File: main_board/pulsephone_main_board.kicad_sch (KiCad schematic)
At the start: 88 parts, among them J1 USB_C_Receptacle_USB2.0_14P, J2 Conn_01x05, J3 Conn_2Rows-35Pins_MountingPin, J4 Conn_2Rows-35Pins_MountingPin, J5 Conn_2Rows-35Pins_MountingPin, J7 Micro_SD_Card_Det1, SW1 SW_Push, SW2 SW_Push, U1 XL1509-3.3, U2 PCM5102APWR, U4 TPS63020DSJR/3.7V Reg, U5 TP4056-42-ESOP8

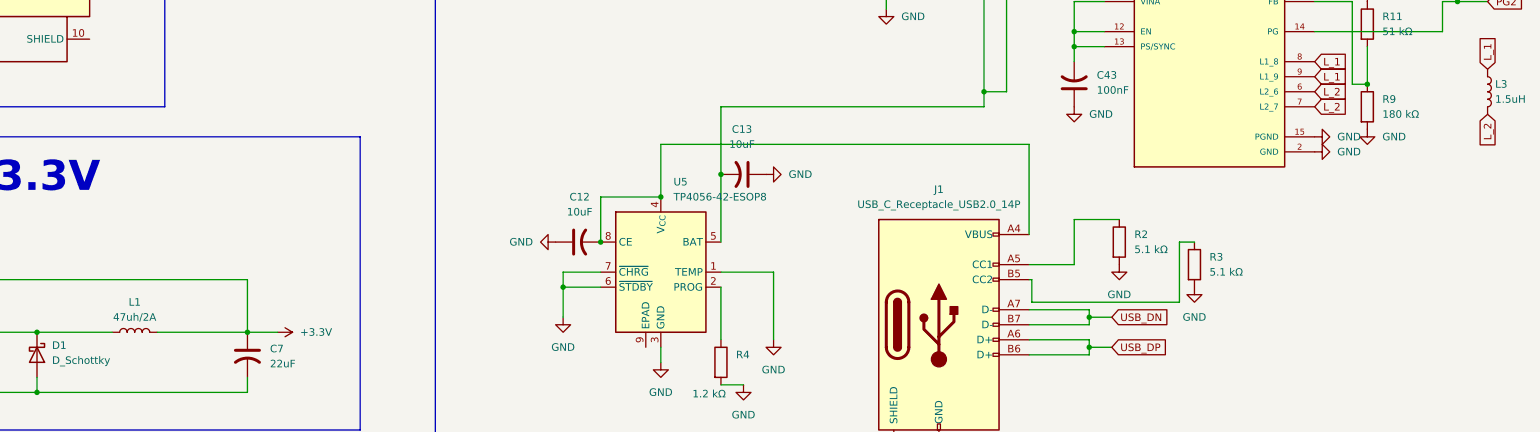
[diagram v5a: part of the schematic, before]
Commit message: footprint size adjustments for better part compatibility when ordering
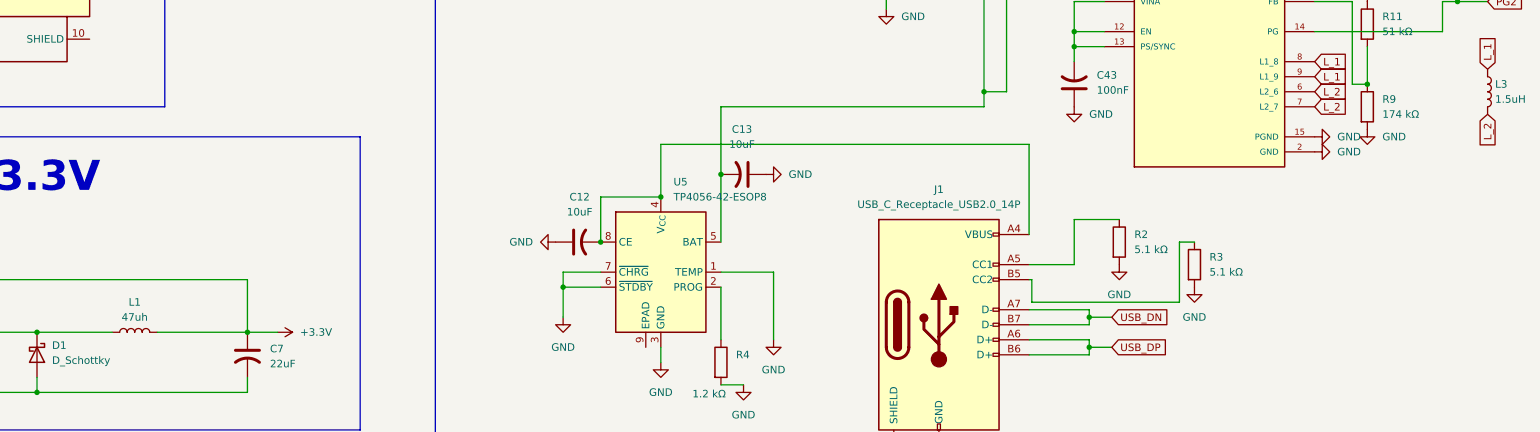
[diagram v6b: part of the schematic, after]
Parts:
- BT1: footprint Connector_PinHeader_1.00mm:PinHeader_1x02_P1.00mm_Horizontal -> Connector_PinHeader_2.54mm:PinHeader_1x02_P2.54mm_Horizontal
- C1, C10, C11, C14, C15, C16, C17, C18, C19, C20, C21, C22, C23, C24, C25, C26, C27, C28, C29, C30, C31, C32, C35, C36, C37, C7, C8, C9: footprint Capacitor_SMD:C_0603_1608Metric -> Capacitor_SMD:C_0805_2012Metric
- J2: footprint Connector_PinHeader_1.00mm:PinHeader_1x05_P1.00mm_Horizontal -> Connector_PinHeader_2.54mm:PinHeader_1x05_P2.54mm_Horizontal
- L1: value 47uh/2A -> 47uh; footprint Inductor_SMD:L_APV_APH0630 -> Inductor_SMD:L_KOHERelec_MDA7030
- R9: value 180 kΩ -> 174 kΩ
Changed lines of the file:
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@@
 			)
 		)
-		(property "Footprint" "Capacitor_SMD:C_0603_1608Metric"
+		(property "Footprint" "Capacitor_SMD:C_0805_2012Metric"
 			(at 458.47 128.27 0)
 			(effects
@@
 			)
 		)
-		(property "Footprint" "Capacitor_SMD:C_0603_1608Metric"
+		(property "Footprint" "Capacitor_SMD:C_0805_2012Metric"
 			(at 505.46 128.27 0)
 			(effects
@@
 			)
 		)
-		(property "Footprint" "Capacitor_SMD:C_0603_1608Metric"
+		(property "Footprint" "Capacitor_SMD:C_0805_2012Metric"
 			(at 792.48 363.22 0)
 			(effects
@@
 			)
 		)
-		(property "Footprint" "Capacitor_SMD:C_0603_1608Metric"
+		(property "Footprint" "Capacitor_SMD:C_0805_2012Metric"
 			(at 600.71 441.96 0)
 			(effects
@@
 			)
 		)
-		(property "Footprint" "Capacitor_SMD:C_0603_1608Metric"
+		(property "Footprint" "Capacitor_SMD:C_0805_2012Metric"
 			(at 712.47 100.33 0)
 			(effects
@@
 			)
 		)
-		(property "Footprint" "Capacitor_SMD:C_0603_1608Metric"
+		(property "Footprint" "Capacitor_SMD:C_0805_2012Metric"
 			(at 792.48 355.6 0)
 			(effects
@@
 			)
 		)
-		(property "Footprint" "Capacitor_SMD:C_0603_1608Metric"
+		(property "Footprint" "Capacitor_SMD:C_0805_2012Metric"
 			(at 429.26 128.27 0)
 			(effects
@@
 			)
 		)
-		(property "Footprint" "Capacitor_SMD:C_0603_1608Metric"
+		(property "Footprint" "Capacitor_SMD:C_0805_2012Metric"
 			(at 533.4 495.3 0)
 			(effects
@@
 			)
 		)
-		(property "Footprint" "Capacitor_SMD:C_0603_1608Metric"
+		(property "Footprint" "Capacitor_SMD:C_0805_2012Metric"
 			(at 534.67 128.27 0)
 			(effects
@@
 			)
 		)
-		(property "Footprint" "Capacitor_SMD:C_0603_1608Metric"
+		(property "Footprint" "Capacitor_SMD:C_0805_2012Metric"
 			(at 726.44 100.33 0)
 			(effects
@@
 			)
 		)
-		(property "Footprint" "Capacitor_SMD:C_0603_1608Metric"
+		(property "Footprint" "Capacitor_SMD:C_0805_2012Metric"
 			(at 741.68 100.33 0)
 			(effects
@@
 			)
 		)
-		(property "Footprint" "Capacitor_SMD:C_0603_1608Metric"
+		(property "Footprint" "Capacitor_SMD:C_0805_2012Metric"
 			(at 792.48 370.84 0)
 			(effects
@@
 			)
 		)
-		(property "Footprint" "Capacitor_SMD:C_0603_1608Metric"
+		(property "Footprint" "Capacitor_SMD:C_0805_2012Metric"
 			(at 473.71 128.27 0)
 			(effects
@@
 			)
 		)
-		(property "Footprint" "Capacitor_SMD:C_0603_1608Metric"
+		(property "Footprint" "Capacitor_SMD:C_0805_2012Metric"
 			(at 590.55 518.16 0)
 			(effects
@@
 			)
 		)
-		(property "Footprint" "Capacitor_SMD:C_0603_1608Metric"
+		(property "Footprint" "Capacitor_SMD:C_0805_2012Metric"
 			(at 651.51 100.33 0)
 			(effects
@@
 			)
 		)
-		(property "Footprint" "Capacitor_SMD:C_0603_1608Metric"
+		(property "Footprint" "Capacitor_SMD:C_0805_2012Metric"
 			(at 665.48 100.33 0)
 			(effects
@@
 			)
 		)
-		(property "Footprint" "Capacitor_SMD:C_0603_1608Metric"
+		(property "Footprint" "Capacitor_SMD:C_0805_2012Metric"
 			(at 636.27 100.33 0)
 			(effects
@@
 			)
 		)
-		(property "Footprint" "Connector_PinHeader_1.00mm:PinHeader_1x02_P1.00mm_Horizontal"
+		(property "Footprint" "Connector_PinHeader_2.54mm:PinHeader_1x02_P2.54mm_Horizontal"
 			(at 708.66 374.396 90)
 			(effects
@@
 			)
 		)
-		(property "Datasheet" "~"
+		(property "Datasheet" ""
 			(at 708.66 374.396 90)
 			(effects
@@
 			)
 		)
-		(property "Description" "Multiple-cell battery"
+		(property "Description" ""
 			(at 708.66 375.92 0)
 			(effects
@@
 			)
 		)
-		(property "Footprint" "Capacitor_SMD:C_0603_1608Metric"
+		(property "Footprint" "Capacitor_SMD:C_0805_2012Metric"
 			(at 444.5 128.27 0)
 			(effects
@@
 			)
 		)
-		(property "Value" "180 kΩ"
+		(property "Value" "174 kΩ"
 			(at 792.48 401.3199 0)
 			(effects
@@
 			)
 		)
-		(property "Footprint" "Capacitor_SMD:C_0603_1608Metric"
+		(property "Footprint" "Capacitor_SMD:C_0805_2012Metric"
 			(at 590.55 502.92 0)
 			(effects
@@
 			)
 		)
-		(property "Footprint" "Capacitor_SMD:C_0603_1608Metric"
+		(property "Footprint" "Capacitor_SMD:C_0805_2012Metric"
 			(at 383.54 128.27 0)
 			(effects
@@
 			)
 		)
-		(property "Footprint" "Capacitor_SMD:C_0603_1608Metric"
+		(property "Footprint" "Capacitor_SMD:C_0805_2012Metric"
 			(at 490.22 128.27 0)
 			(effects
@@
 			)
 		)
-		(property "Footprint" "Capacitor_SMD:C_0603_1608Metric"
+		(property "Footprint" "Capacitor_SMD:C_0805_2012Metric"
 			(at 590.55 510.54 0)
 			(effects
@@
 			)
 		)
-		(property "Footprint" "Capacitor_SMD:C_0603_1608Metric"
+		(property "Footprint" "Capacitor_SMD:C_0805_2012Metric"
 			(at 397.51 128.27 0)
 			(effects
@@
 			)
 		)
-		(property "Footprint" "Connector_PinHeader_1.00mm:PinHeader_1x05_P1.00mm_Horizontal"
+		(property "Footprint" "Connector_PinHeader_2.54mm:PinHeader_1x05_P2.54mm_Horizontal"
 			(at 289.56 359.41 0)
 			(effects
@@
 			)
 		)
-		(property "Datasheet" "~"
+		(property "Datasheet" ""
 			(at 289.56 359.41 0)
 			(effects
@@
 			)
 		)
-		(property "Description" "Generic connector, single row, 01x05, script generated (kicad-library-utils/schlib/autogen/connector/)"
+		(property "Description" ""
 			(at 289.56 359.41 0)
 			(effects
@@
 			)
 		)
-		(property "Footprint" "Capacitor_SMD:C_0603_1608Metric"
+		(property "Footprint" "Capacitor_SMD:C_0805_2012Metric"
 			(at 521.97 441.96 0)
 			(effects
@@
 			)
 		)
-		(property "Footprint" "Capacitor_SMD:C_0603_1608Metric"
+		(property "Footprint" "Capacitor_SMD:C_0805_2012Metric"
 			(at 519.43 128.27 0)
 			(effects
@@
 			)
 		)
-		(property "Footprint" "Capacitor_SMD:C_0603_1608Metric"
+		(property "Footprint" "Capacitor_SMD:C_0805_2012Metric"
 			(at 412.75 128.27 0)
 			(effects
@@
 			)
 		)
-		(property "Footprint" "Capacitor_SMD:C_0603_1608Metric"
+		(property "Footprint" "Capacitor_SMD:C_0805_2012Metric"
 			(at 680.72 100.33 0)
 			(effects
@@
 			)
 		)
-		(property "Value" "47uh/2A"
+		(property "Value" "47uh"
 			(at 581.66 435.61 90)
 			(effects
@@
 			)
 		)
-		(property "Footprint" "Inductor_SMD:L_APV_APH0630"
+		(property "Footprint" "Inductor_SMD:L_KOHERelec_MDA7030"
 			(at 581.66 438.15 0)
 			(effects
@@
 			)
 		)
-		(property "Datasheet" "~"
+		(property "Datasheet" ""
 			(at 581.66 438.15 0)
 			(effects
@@
 			)
 		)
-		(property "Description" "Inductor"
+		(property "Description" ""
 			(at 581.66 438.15 0)
 			(effects
@@
 			)
 		)
-		(property "Footprint" "Capacitor_SMD:C_0603_1608Metric"
+		(property "Footprint" "Capacitor_SMD:C_0805_2012Metric"
 			(at 697.23 100.33 0)
 			(effects

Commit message: final review change (board was ordered, prod ready verSion)
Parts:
- added AUD-L1, AUD-R1: TestPoint, TestPoint:TestPoint_Pad_1.0x1.0mm, symbol Connector:TestPoint
- added I2C3-SCL1, I2C3-SDA1: TestPoint, TestPoint:TestPoint_Pad_D1.0mm, symbol Connector:TestPoint
- 3.3V1, 5V1, CLK-N1, CLK-P1, D0-N1, D0-P1, D1-N1, D1-P1, D2-N1, D2-P1, D3-N1, D3-P1, GND1, VBAT1: footprint TestPoint:TestPoint_Pad_1.0x1.0mm -> TestPoint:TestPoint_Pad_D1.0mm
- J1: footprint Connector_USB:USB_C_Receptacle_Amphenol_12401548E4-2A -> Connector_USB:USB_C_Receptacle_HRO_TYPE-C-31-M-12
- ON/OFF1: renamed from SW2; footprint Button_Switch_SMD:SW_Tactile_SPST_NO_Straight_CK_PTS636Sx25SMTRLFS -> SSSS810701:SSSS810701; symbol Switch:SW_Push -> SSSS810701:SSSS810701; Availability (none) -> In Stock; Check_prices (none) -> https://www.snapeda.com/parts/SSSS810701/ALPS/view-part/?re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; Description_1 (none) -> Slide Switch • Rating (max.): 0.3 A 5 VDC • Poles: 1 • Posi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; MF (none) -> ALPS; MP (none) -> SSSS810701; Package (none) -> None; Price (none) -> None; SnapEDA_Link (none) -> https://www.snapeda.com/parts/SSSS810701/ALPS/view-part/?re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
- RESET1: renamed from SW1; footprint Button_Switch_SMD:SW_Tactile_SPST_NO_Straight_CK_PTS636Sx25SMTRLFS -> Button_Switch_SMD:SW_Push_1P1T-SH_NO_CK_KMR2xxG
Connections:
- net GND: now also J1.S1 (SHIELD), J7.10 (SHIELD), U5.9 (EPAD)
- net GNDCHASSIS: no longer J1.S1 (SHIELD)
- net I2C3_SCL: now also I2C3-SCL1.1
- net I2C3_SDA: now also I2C3-SDA1.1
- net ONOFF: now also ON/OFF1.3; no longer ON/OFF1.2
- net at J5.8 (Pin_8), U2.6 (OUTL): now also AUD-L1.1
- net at J5.9 (Pin_9), U2.7 (OUTR): now also AUD-R1.1
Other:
- moved on the sheet: ON/OFF1

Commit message: restart project for summer, misc changes
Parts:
- removed D1: D_Schottky, Diode_SMD:D_SMA, symbol Device:D_Schottky
- removed L1: 47uh, Inductor_SMD:L_KOHERelec_MDA7030, symbol Device:L
- removed U1: XL1509-3.3, Package_SO:SOIC-8_3.9x4.9mm_P1.27mm, symbol Regulator_Switching:XL1509-3.3
- added J6: Conn_01x01_Socket, Connector_Coaxial:U.FL_Hirose_U.FL-R-SMT-1_Vertical, symbol Connector:Conn_01x01_Socket
- added R12: 10 kΩ, Resistor_SMD:R_0805_2012Metric, symbol Device:R
- added U1: AP2112K-3.3, Package_TO_SOT_SMD:SOT-23-5, symbol Regulator_Linear:AP2112K-3.3
- added U6: LBEE5KL1YN-814, footprints:XCVR_LBEE5KL1YN-814, symbol LBEE5KL1YN-814:LBEE5KL1YN-814
- added Y1: XO53, Oscillator:Oscillator_SMD_EuroQuartz_XO53-4Pin_5.0x3.2mm, symbol Oscillator:XO53
- 3.3V1, 5V1, CLK-N1, CLK-P1, D0-N1, D0-P1, D1-N1, D1-P1, D2-N1, D2-P1, D3-N1, D3-P1, GND1, I2C3-SCL1, I2C3-SDA1, VBAT1: footprint TestPoint:TestPoint_Pad_D1.0mm -> TestPoint:TestPoint_Pad_D2.5mm
- C1, C7: value 22uF -> 1uF; footprint Capacitor_SMD:C_0805_2012Metric -> Capacitor_SMD:C_0603_1608Metric
- C14, C15, C16, C17, C18, C19: value 22uF -> 100nF
- ON/OFF1: value SW_Push -> SSSS810701
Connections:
- net +3.3V: now also C7.2, R12.1, U1.5 (VOUT), Y1.1 (EN), Y1.4 (V+); no longer C7.1
- net +5V: now also C1.2, U1.1 (VIN), U1.3 (EN); no longer C1.1
- net GND: now also C1.1, C7.1, U2.17 (XSMT), R12.2, U1.2 (GND), U6.1 (GND), U6.12 (GND), U6.19 (GND), U6.21 (GND), U6.29 (GND), U6.32 (GND(SR_PVSS)), U6.33 (GND(SR_PVSS)), U6.35 (GND), U6.40 (GND), U6.42 (GND), U6.43 (GND), U6.44 (GND), U6.45 (GND), U6.46 (GND), Y1.2 (GND); no longer C1.2, C7.2
- net BT_UART_RTS_N: now reaches MCM93_MOD1.100 (30)
- net BT_UART_RTS_N: now also U6.5 (BT_UART_RTS_N)
- net BT_UART_CTS_N: now reaches MCM93_MOD1.101 (31)
- net BT_UART_CTS_N: now also U6.4 (BT_UART_CTS_N)
- net BT_UART_R: now reaches MCM93_MOD1.102 (32)
- net BT_UART_R: now also U6.2 (BT_UART_RXD)
- net BT_UART_T: now reaches MCM93_MOD1.103 (33)
- net BT_UART_T: now also U6.3 (BT_UART_TXD)
- net REG_ON_WL: now reaches MCM93_MOD1.104 (34)
- net REG_ON_WL: now also U6.28 (WL_REG_ON)
- net REG_ON_BL: now reaches MCM93_MOD1.105 (35)
- net REG_ON_BL: now also U6.14 (BT_REG_ON)
- net GPIO_WF_2: now reaches MCM93_MOD1.85 (15)
- net GPIO_WF_2: now also U6.17 (WL_GPIO_2)
- net GPIO_WF_1: now reaches MCM93_MOD1.93 (23)
- net GPIO_WF_1: now also U6.18 (WL_GPIO_1)
- net GPIO_WF_0: now reaches MCM93_MOD1.94 (24)
- net GPIO_WF_0: now also U6.27 (WL_GPIO_0_HOST_WAKE)
- net SDIO_CLK: now reaches MCM93_MOD1.109 (4)
- net SDIO_CLK: now also U6.20 (SDIO_CLK)
- net SDIO_2: now reaches MCM93_MOD1.110 (5)
- net SDIO_2: now also U6.23 (SDIO_DATA_2)
- net SDIO_3: now reaches MCM93_MOD1.111 (6)
- net SDIO_3: now also U6.25 (SDIO_DATA_3)
- net SDIO_1: now reaches MCM93_MOD1.112 (7)
- net SDIO_1: now also U6.26 (SDIO_DATA_1)
- net SDIO_CMD: now reaches MCM93_MOD1.113 (8)
- net SDIO_CMD: now also U6.22 (SDIO_CMD)
- net SDIO_0: now reaches MCM93_MOD1.114 (9)
- net SDIO_0: now also U6.24 (SDIO_DATA_0)
- net PCM_OUT: now reaches MCM93_MOD1.51 (16)
- net PCM_OUT: now also U6.10 (BT_PCM_OUT)
- net PCM_SYNC: now reaches MCM93_MOD1.54 (19)
- net PCM_SYNC: now also U6.8 (BT_PCM_SYNC)
- net PCM_CLK: now reaches MCM93_MOD1.56 (21)
- net PCM_CLK: now also U6.11 (BT_PCM_CLK)
- net PCM_IN: now reaches MCM93_MOD1.58 (23)
- net PCM_IN: now also U6.9 (BT_PCM_IN)
- new net: J6.1 (Pin_1), U6.41 (ANT)
- new net: U6.13 (NC), U6.15 (NC), U6.16 (NC), U6.6 (NC), U6.7 (NC)
- new net: U6.37 (LPO_IN(32KHZ)), Y1.3 (OUT)
- new net DEV_WAKE: U6.39 (BT_DEV_WAKE)
- new net HOST_WAKE: U6.38 (BT_HOST_WAKE)
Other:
- note added: "WIFI/BT"
- moved on the sheet: C12
